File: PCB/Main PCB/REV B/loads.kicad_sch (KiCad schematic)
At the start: 13 parts

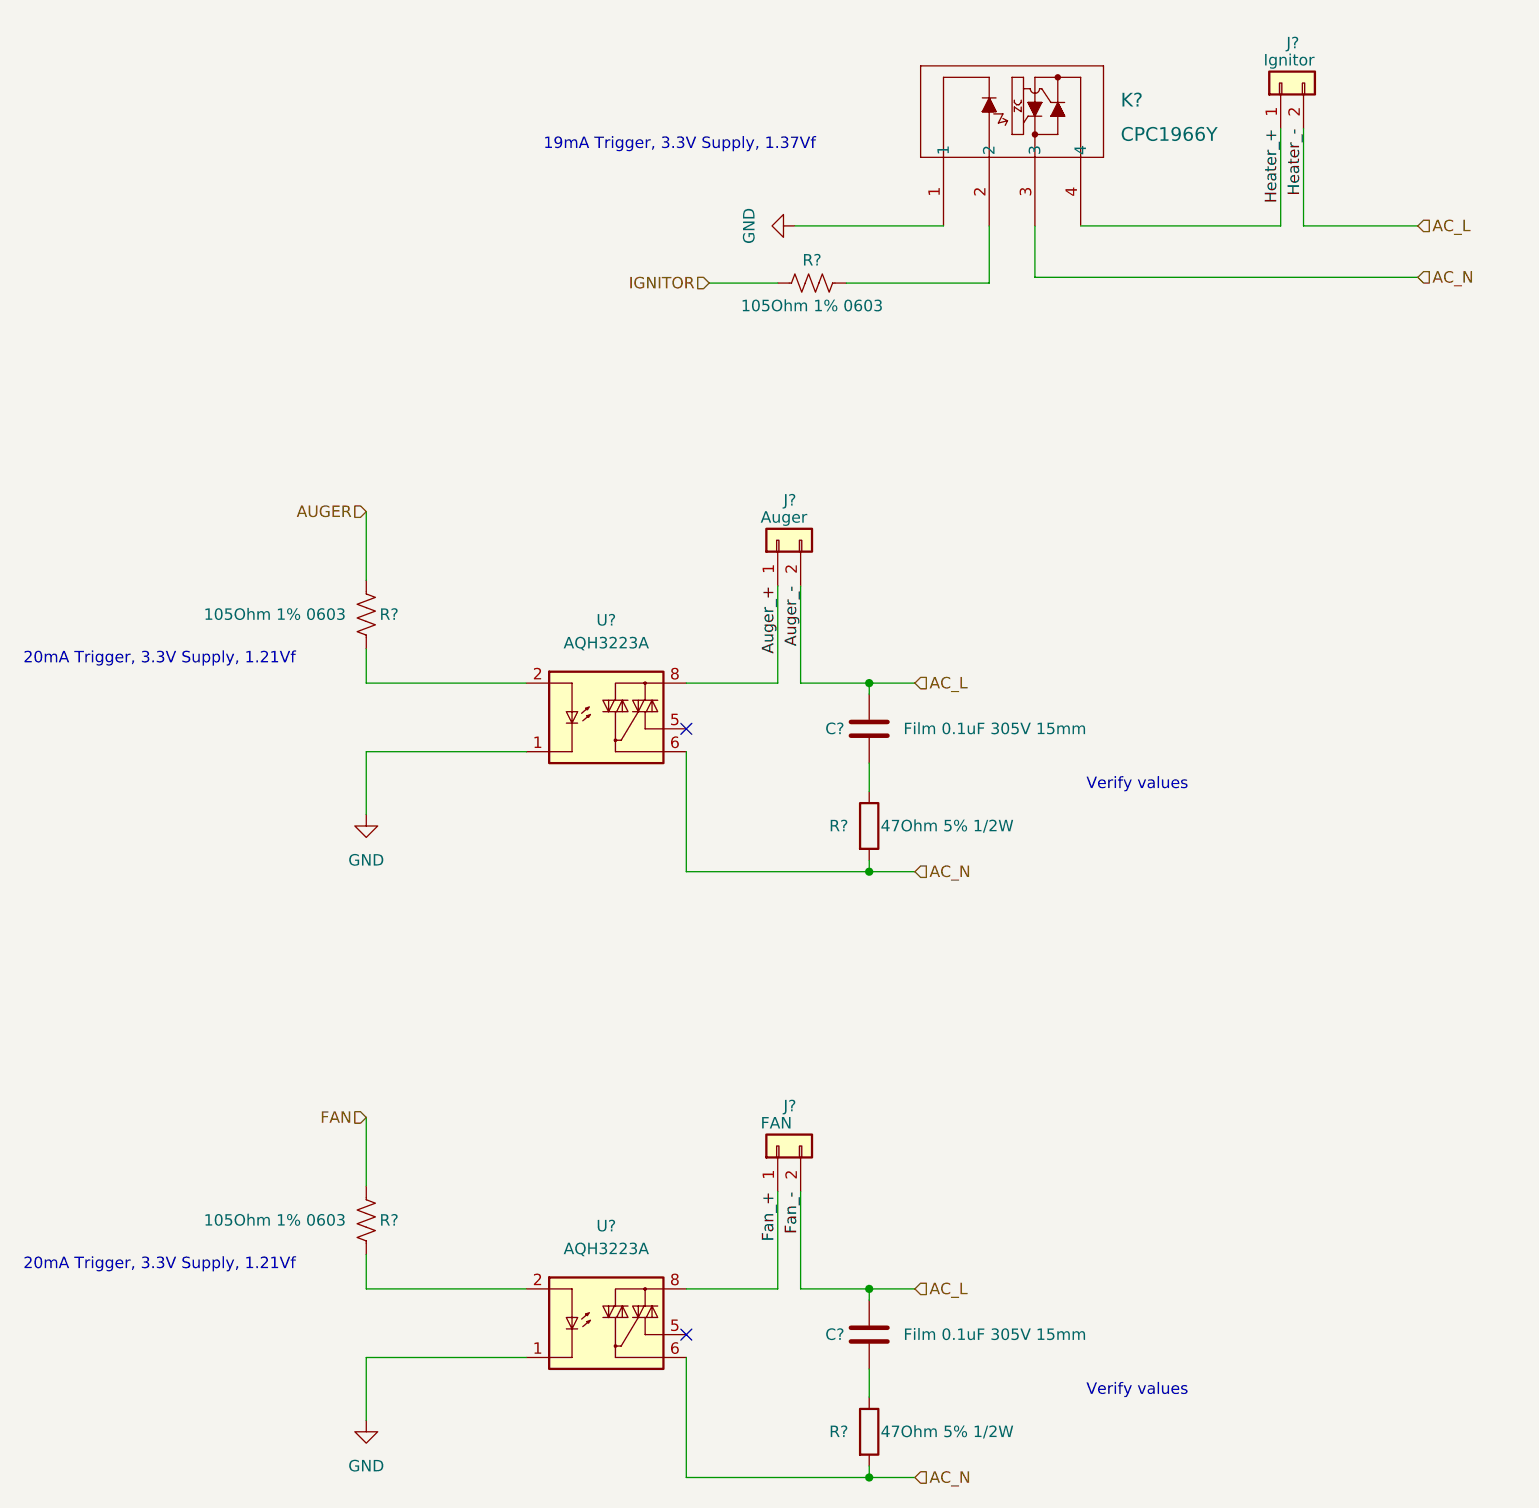
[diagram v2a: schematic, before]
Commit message: Rid power path selector, moving to or diode system for power path selection
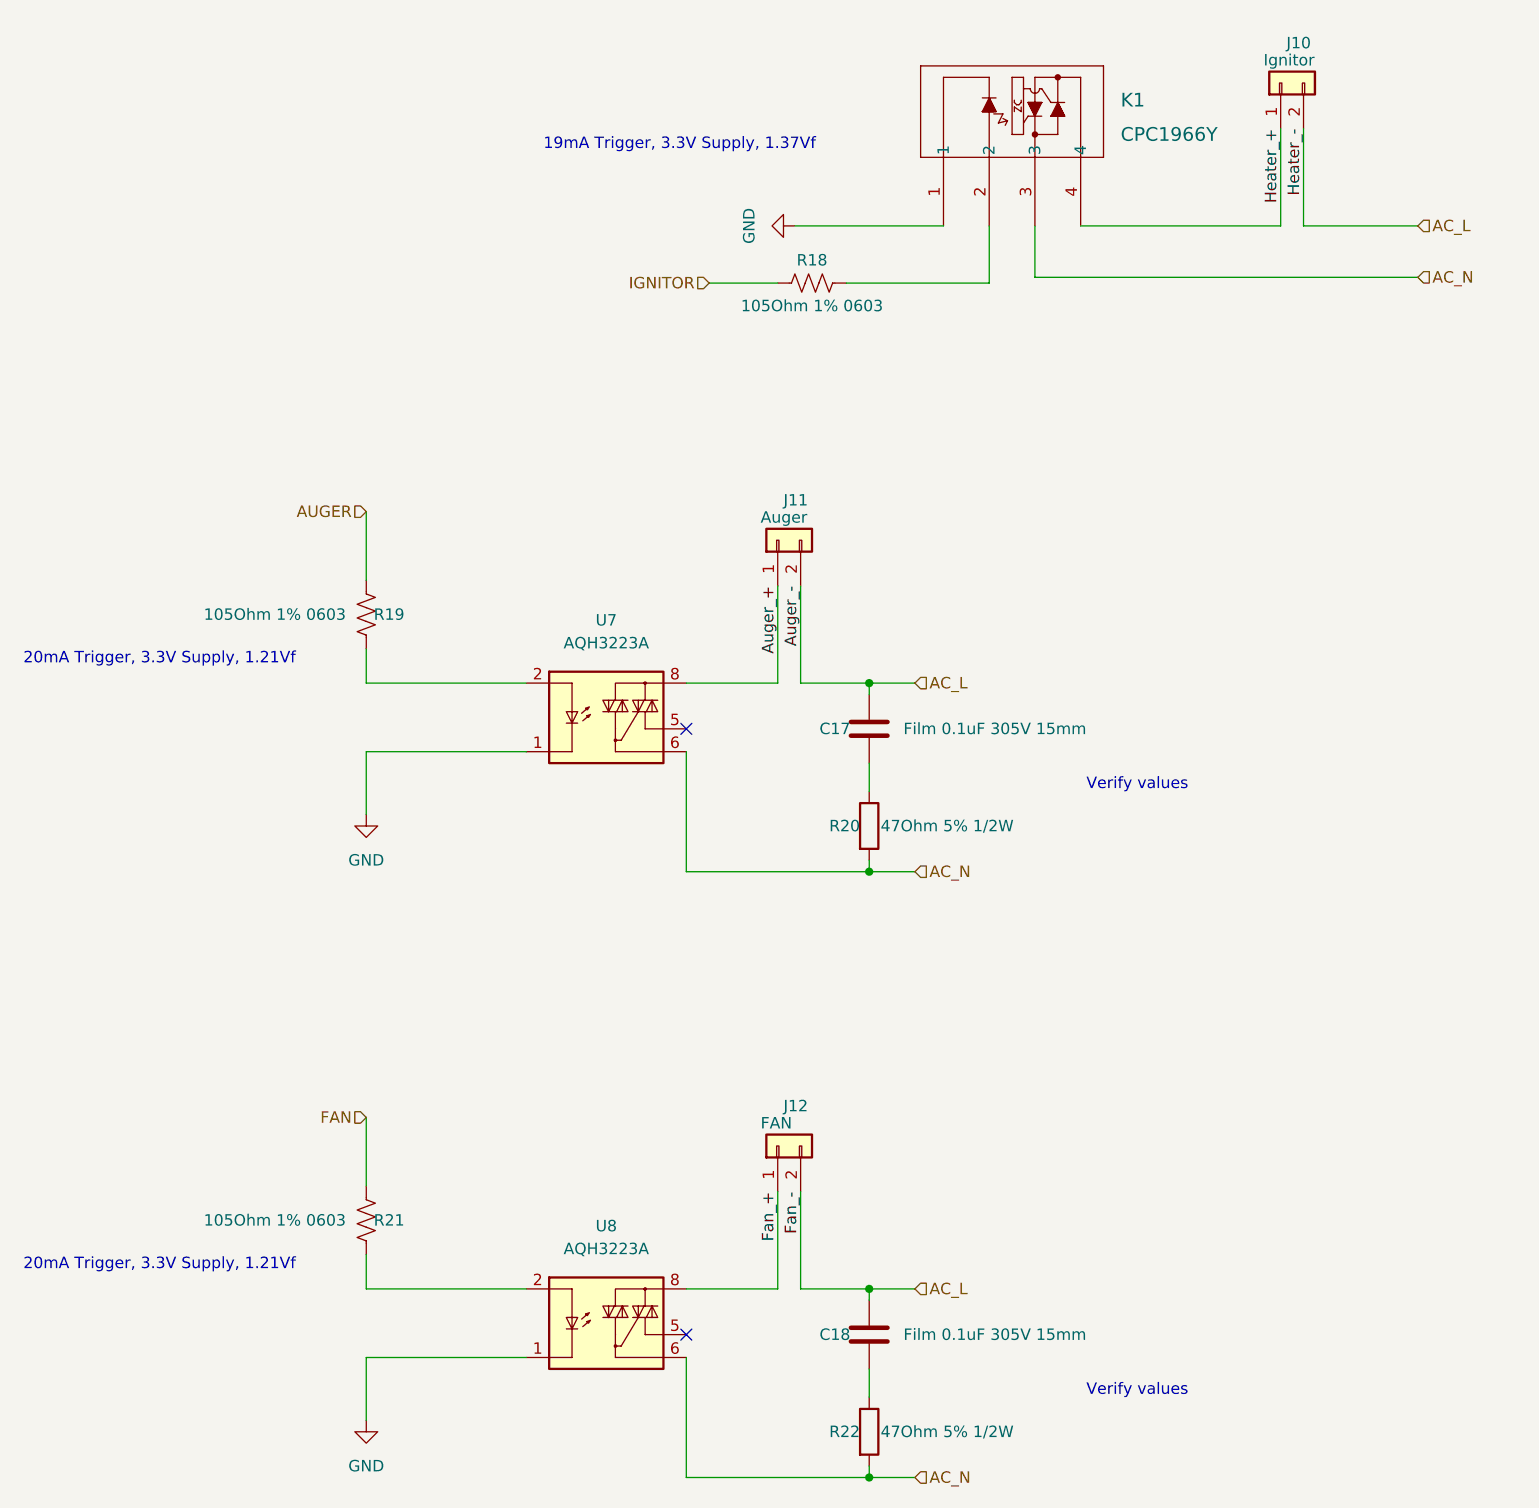
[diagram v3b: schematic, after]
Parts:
- gave numbers to parts that had none: 13
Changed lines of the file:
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@@
   (symbol (lib_id "Connector_Generic:Conn_01x02") (at 120.65 153.67 90) (unit 1)
     (in_bom yes) (on_board yes)
-    (property "Reference" "J?" (id 0) (at 121.285 149.225 90)
+    (property "Reference" "J12" (id 0) (at 121.285 149.225 90)
       (effects (font (size 1.27 1.27)) (justify right))
     )
@@
   (symbol (lib_id "Relay_SolidState:AQH3223A") (at 102.87 172.085 0) (unit 1)
     (in_bom yes) (on_board yes) (fields_autoplaced)
-    (property "Reference" "U?" (id 0) (at 101.6 162.56 0))
+    (property "Reference" "U8" (id 0) (at 101.6 162.56 0))
     (property "Value" "AQH3223A" (id 1) (at 101.6 165.1 0))
     (property "Footprint" "Package_SO:SSO-7-8_6.4x9.78mm_P2.54mm" (id 2) (at 95.25 177.165 0)
@@
   (symbol (lib_id "Device:C") (at 130.81 107.315 0) (unit 1)
     (in_bom yes) (on_board yes)
-    (property "Reference" "C?" (id 0) (at 127 107.315 0))
+    (property "Reference" "C17" (id 0) (at 127 107.315 0))
     (property "Value" "Film 0.1uF 305V 15mm" (id 1) (at 144.78 107.315 0))
     (property "Footprint" "Capacitor_THT:C_Rect_L18.0mm_W6.0mm_P15.00mm_FKS3_FKP3" (id 2) (at 131.7752 111.125 0)
@@
   (symbol (lib_id "Device:C") (at 130.81 174.625 0) (unit 1)
     (in_bom yes) (on_board yes)
-    (property "Reference" "C?" (id 0) (at 127 174.625 0))
+    (property "Reference" "C18" (id 0) (at 127 174.625 0))
     (property "Value" "Film 0.1uF 305V 15mm" (id 1) (at 144.78 174.625 0))
     (property "Footprint" "Capacitor_THT:C_Rect_L18.0mm_W6.0mm_P15.00mm_FKS3_FKP3" (id 2) (at 131.7752 178.435 0)
@@
   (symbol (lib_id "Relay_SolidState:AQH3223A") (at 102.87 104.775 0) (unit 1)
     (in_bom yes) (on_board yes) (fields_autoplaced)
-    (property "Reference" "U?" (id 0) (at 101.6 95.25 0))
+    (property "Reference" "U7" (id 0) (at 101.6 95.25 0))
     (property "Value" "AQH3223A" (id 1) (at 101.6 97.79 0))
     (property "Footprint" "Package_SO:SSO-7-8_6.4x9.78mm_P2.54mm" (id 2) (at 95.25 109.855 0)
@@
   (symbol (lib_id "CPC1966Y:CPC1966Y") (at 139.065 51.435 90) (unit 1)
     (in_bom yes) (on_board yes) (fields_autoplaced)
-    (property "Reference" "K?" (id 0) (at 158.75 37.465 90)
+    (property "Reference" "K1" (id 0) (at 158.75 37.465 90)
       (effects (font (size 1.524 1.524)) (justify right))
     )
@@
   (symbol (lib_id "Device:R") (at 130.81 118.11 0) (unit 1)
     (in_bom yes) (on_board yes)
-    (property "Reference" "R?" (id 0) (at 126.365 118.11 0)
+    (property "Reference" "R20" (id 0) (at 126.365 118.11 0)
       (effects (font (size 1.27 1.27)) (justify left))
     )
@@
   (symbol (lib_id "power:GND") (at 74.93 116.84 0) (mirror y) (unit 1)
     (in_bom yes) (on_board yes)
-    (property "Reference" "#PWR?" (id 0) (at 74.93 123.19 0)
+    (property "Reference" "#PWR060" (id 0) (at 74.93 123.19 0)
       (effects (font (size 1.27 1.27)) hide)
     )
@@
   (symbol (lib_id "Device:R_US") (at 74.93 161.925 0) (unit 1)
     (in_bom yes) (on_board yes)
-    (property "Reference" "R?" (id 0) (at 77.47 161.925 0))
+    (property "Reference" "R21" (id 0) (at 77.47 161.925 0))
     (property "Value" "105Ohm 1% 0603" (id 1) (at 64.77 161.925 0))
     (property "Footprint" "Resistor_SMD:R_0603_1608Metric" (id 2) (at 75.946 162.179 90)
@@
   (symbol (lib_id "power:GND") (at 74.93 184.15 0) (mirror y) (unit 1)
     (in_bom yes) (on_board yes)
-    (property "Reference" "#PWR?" (id 0) (at 74.93 190.5 0)
+    (property "Reference" "#PWR061" (id 0) (at 74.93 190.5 0)
       (effects (font (size 1.27 1.27)) hide)
     )
@@
   (symbol (lib_id "Device:R") (at 130.81 185.42 0) (unit 1)
     (in_bom yes) (on_board yes)
-    (property "Reference" "R?" (id 0) (at 126.365 185.42 0)
+    (property "Reference" "R22" (id 0) (at 126.365 185.42 0)
       (effects (font (size 1.27 1.27)) (justify left))
     )
@@
   (symbol (lib_id "Device:R_US") (at 74.93 94.615 0) (unit 1)
     (in_bom yes) (on_board yes)
-    (property "Reference" "R?" (id 0) (at 77.47 94.615 0))
+    (property "Reference" "R19" (id 0) (at 77.47 94.615 0))
     (property "Value" "105Ohm 1% 0603" (id 1) (at 64.77 94.615 0))
     (property "Footprint" "Resistor_SMD:R_0603_1608Metric" (id 2) (at 75.946 94.869 90)
@@
   (symbol (lib_id "Device:R_US") (at 124.46 57.785 90) (unit 1)
     (in_bom yes) (on_board yes)
-    (property "Reference" "R?" (id 0) (at 124.46 55.245 90))
+    (property "Reference" "R18" (id 0) (at 124.46 55.245 90))
     (property "Value" "105Ohm 1% 0603" (id 1) (at 124.46 60.325 90))
     (property "Footprint" "Resistor_SMD:R_0603_1608Metric" (id 2) (at 124.714 56.769 90)
@@
   (symbol (lib_id "Connector_Generic:Conn_01x02") (at 176.53 35.56 90) (unit 1)
     (in_bom yes) (on_board yes)
-    (property "Reference" "J?" (id 0) (at 177.165 31.115 90)
+    (property "Reference" "J10" (id 0) (at 177.165 31.115 90)
       (effects (font (size 1.27 1.27)) (justify right))
     )
@@
   (symbol (lib_id "power:GND") (at 122.555 51.435 270) (mirror x) (unit 1)
     (in_bom yes) (on_board yes)
-    (property "Reference" "#PWR?" (id 0) (at 116.205 51.435 0)
+    (property "Reference" "#PWR059" (id 0) (at 116.205 51.435 0)
       (effects (font (size 1.27 1.27)) hide)
     )
@@
   (symbol (lib_id "Connector_Generic:Conn_01x02") (at 120.65 86.36 90) (unit 1)
     (in_bom yes) (on_board yes)
-    (property "Reference" "J?" (id 0) (at 121.285 81.915 90)
-      (effects (font (size 1.27 1.27)) (justify right))
-    )
+    (property "Reference" "J11" (id 0) (at 121.285 81.915 90)
+      (effects (font (size 1.27 1.27)) (justify right))
+    )

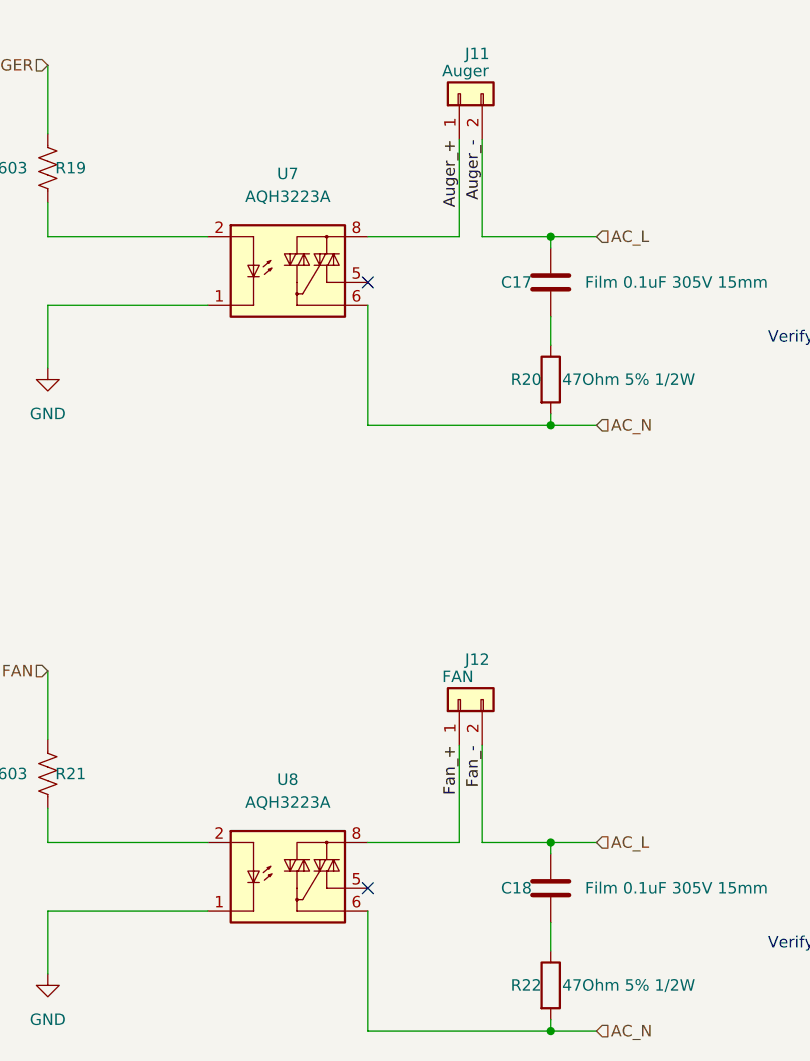
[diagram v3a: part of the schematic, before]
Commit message: Moved from ORing diodes to power MUX as per TI recommendations
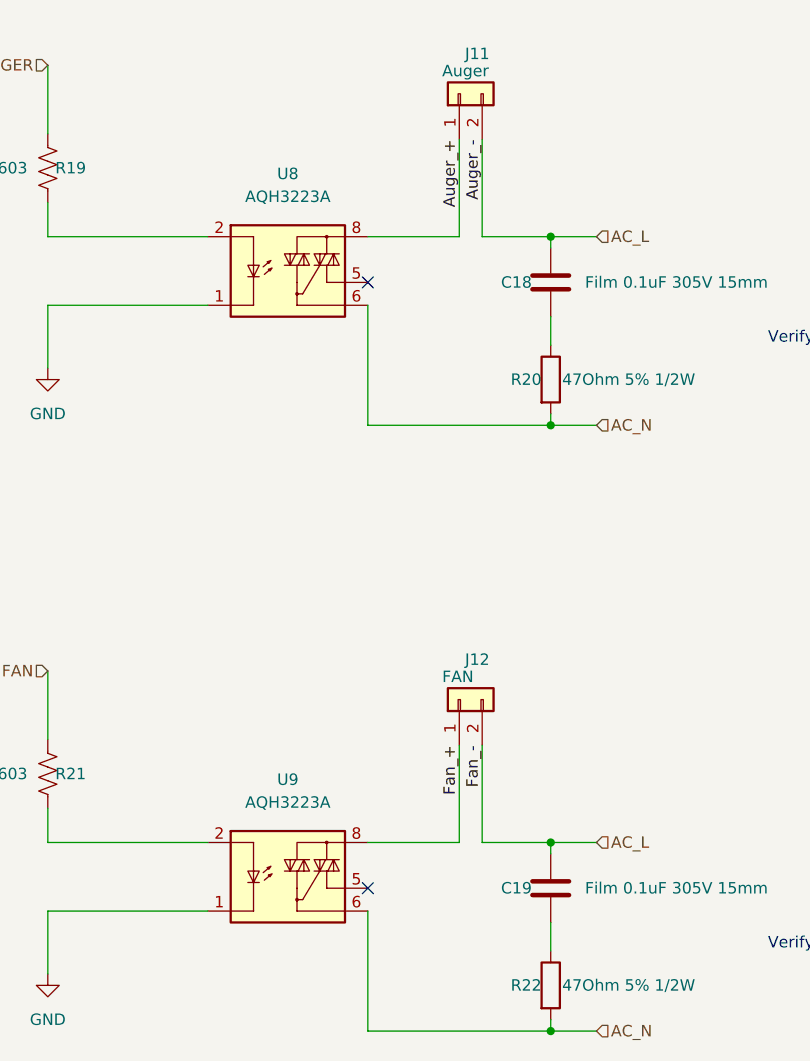
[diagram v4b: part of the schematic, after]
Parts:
- renumbered C17 to C18, C18 to C19, U7 to U8, U8 to U9
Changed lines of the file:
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@@
   (symbol (lib_id "Relay_SolidState:AQH3223A") (at 102.87 172.085 0) (unit 1)
     (in_bom yes) (on_board yes) (fields_autoplaced)
-    (property "Reference" "U8" (id 0) (at 101.6 162.56 0))
+    (property "Reference" "U9" (id 0) (at 101.6 162.56 0))
     (property "Value" "AQH3223A" (id 1) (at 101.6 165.1 0))
     (property "Footprint" "Package_SO:SSO-7-8_6.4x9.78mm_P2.54mm" (id 2) (at 95.25 177.165 0)
@@
   (symbol (lib_id "Device:C") (at 130.81 107.315 0) (unit 1)
     (in_bom yes) (on_board yes)
-    (property "Reference" "C17" (id 0) (at 127 107.315 0))
+    (property "Reference" "C18" (id 0) (at 127 107.315 0))
     (property "Value" "Film 0.1uF 305V 15mm" (id 1) (at 144.78 107.315 0))
     (property "Footprint" "Capacitor_THT:C_Rect_L18.0mm_W6.0mm_P15.00mm_FKS3_FKP3" (id 2) (at 131.7752 111.125 0)
@@
   (symbol (lib_id "Device:C") (at 130.81 174.625 0) (unit 1)
     (in_bom yes) (on_board yes)
-    (property "Reference" "C18" (id 0) (at 127 174.625 0))
+    (property "Reference" "C19" (id 0) (at 127 174.625 0))
     (property "Value" "Film 0.1uF 305V 15mm" (id 1) (at 144.78 174.625 0))
     (property "Footprint" "Capacitor_THT:C_Rect_L18.0mm_W6.0mm_P15.00mm_FKS3_FKP3" (id 2) (at 131.7752 178.435 0)
@@
   (symbol (lib_id "Relay_SolidState:AQH3223A") (at 102.87 104.775 0) (unit 1)
     (in_bom yes) (on_board yes) (fields_autoplaced)
-    (property "Reference" "U7" (id 0) (at 101.6 95.25 0))
+    (property "Reference" "U8" (id 0) (at 101.6 95.25 0))
     (property "Value" "AQH3223A" (id 1) (at 101.6 97.79 0))
     (property "Footprint" "Package_SO:SSO-7-8_6.4x9.78mm_P2.54mm" (id 2) (at 95.25 109.855 0)
@@
   (symbol (lib_id "power:GND") (at 74.93 116.84 0) (mirror y) (unit 1)
     (in_bom yes) (on_board yes)
-    (property "Reference" "#PWR060" (id 0) (at 74.93 123.19 0)
+    (property "Reference" "#PWR061" (id 0) (at 74.93 123.19 0)
       (effects (font (size 1.27 1.27)) hide)
     )
@@
   (symbol (lib_id "power:GND") (at 74.93 184.15 0) (mirror y) (unit 1)
     (in_bom yes) (on_board yes)
-    (property "Reference" "#PWR061" (id 0) (at 74.93 190.5 0)
+    (property "Reference" "#PWR062" (id 0) (at 74.93 190.5 0)
       (effects (font (size 1.27 1.27)) hide)
     )
@@
   (symbol (lib_id "power:GND") (at 122.555 51.435 270) (mirror x) (unit 1)
     (in_bom yes) (on_board yes)
-    (property "Reference" "#PWR059" (id 0) (at 116.205 51.435 0)
-      (effects (font (size 1.27 1.27)) hide)
-    )
+    (property "Reference" "#PWR060" (id 0) (at 116.205 51.435 0)
+      (effects (font (size 1.27 1.27)) hide)
+    )
